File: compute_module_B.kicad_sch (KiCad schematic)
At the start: 3 parts

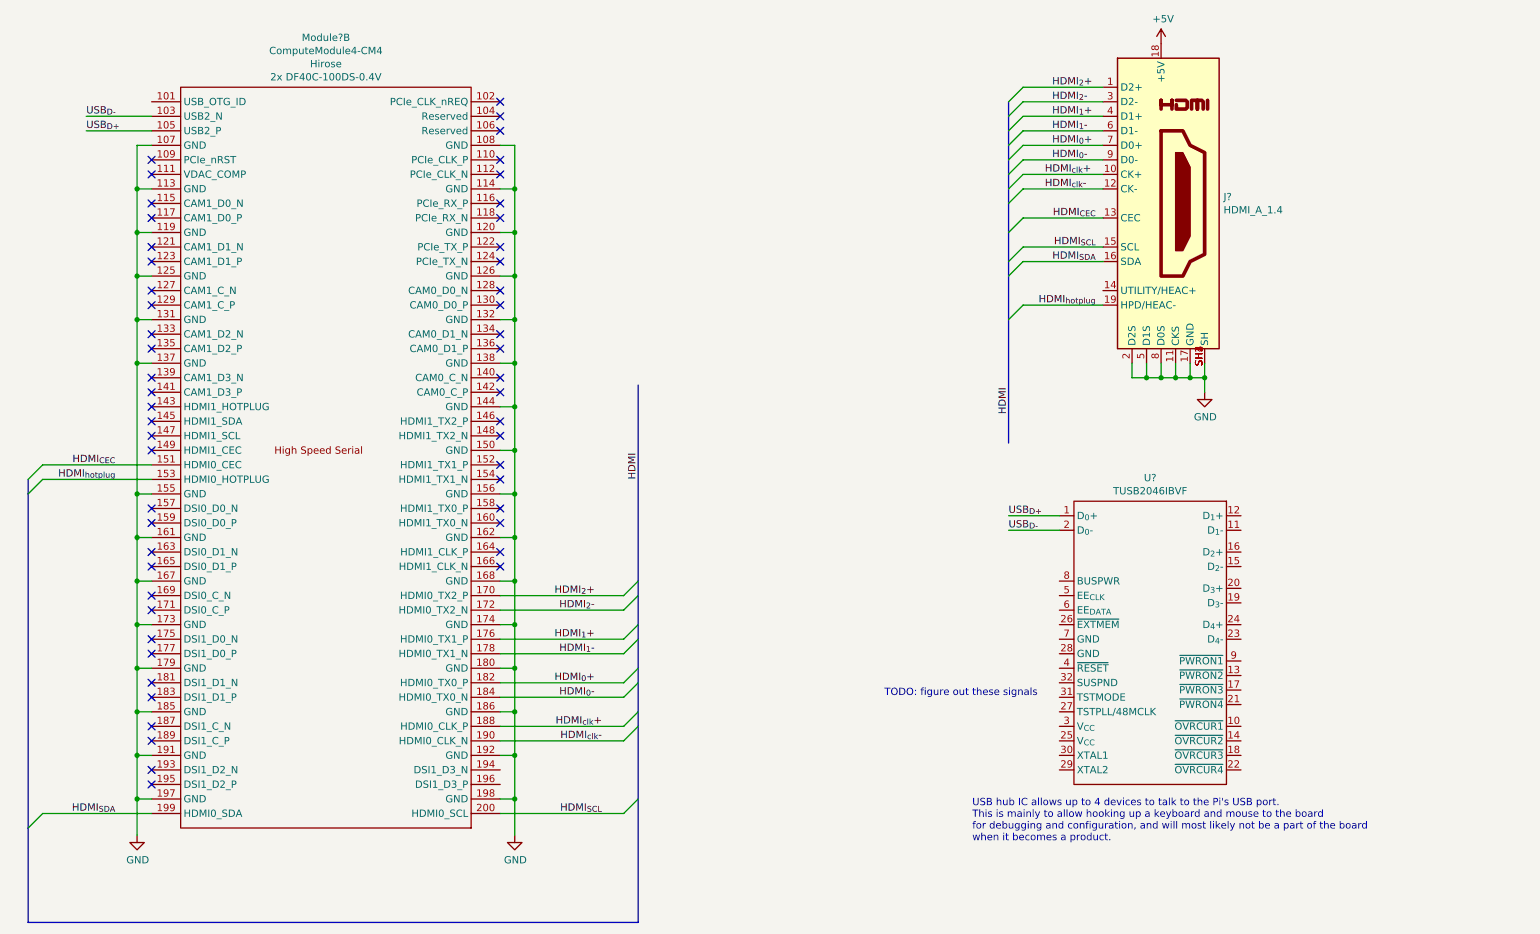
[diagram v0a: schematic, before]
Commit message: Added buses and USB ports to schematic
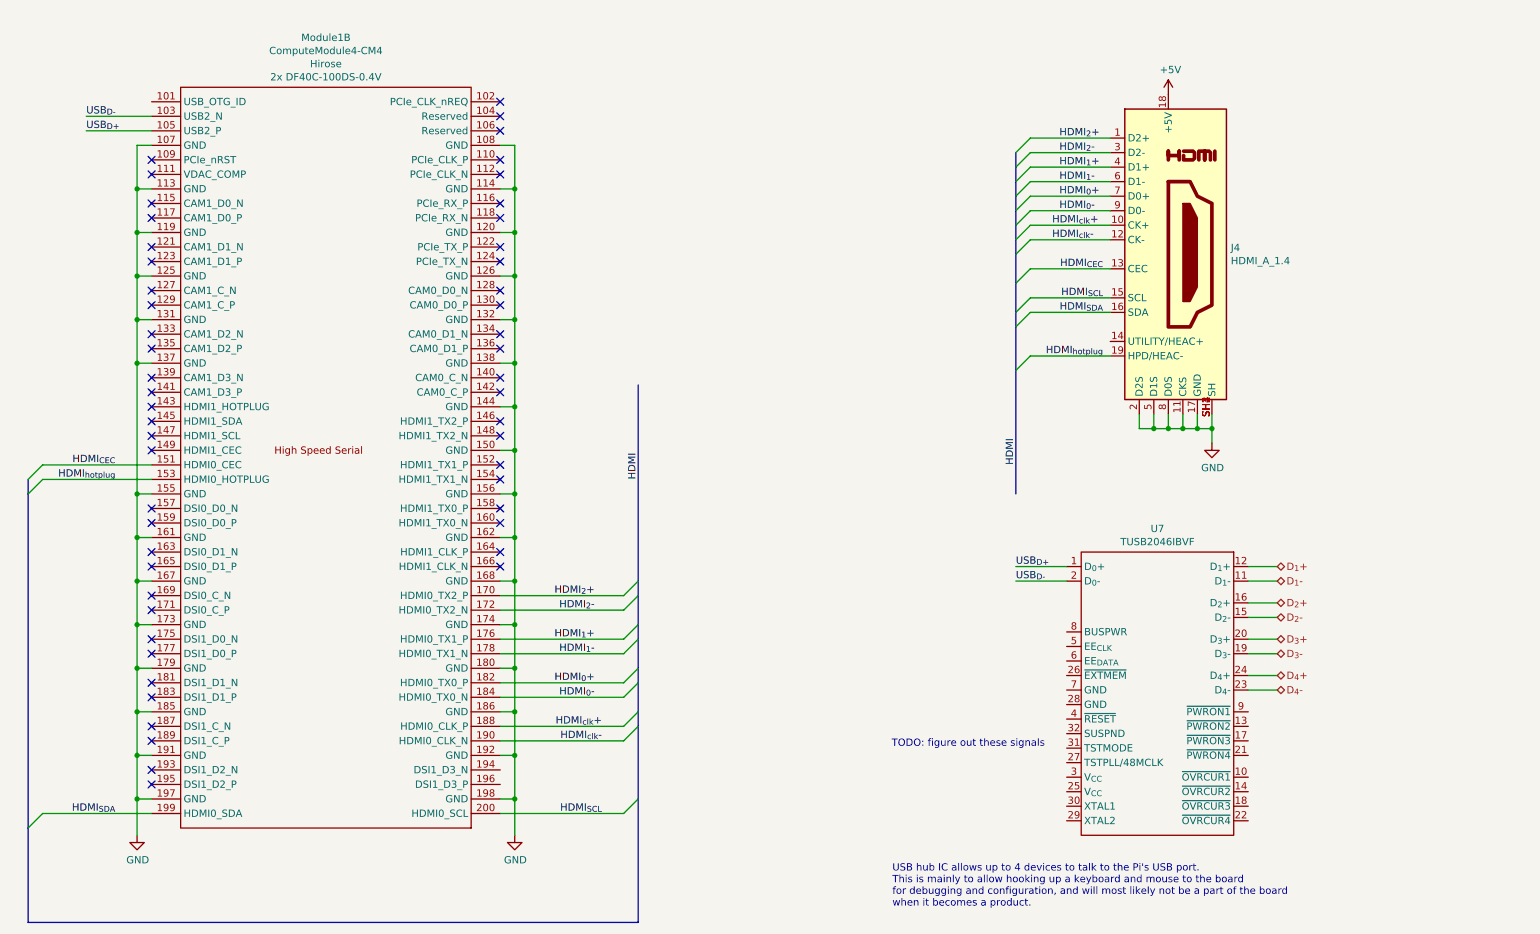
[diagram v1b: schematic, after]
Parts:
- gave numbers to parts that had none: 3
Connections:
- net D_{1}-: now reaches U7.11 (D_{1}-)
- net D_{1}+: now reaches U7.12 (D_{1}+)
- net D_{2}-: now reaches U7.15 (D_{2}-)
- net D_{2}+: now reaches U7.16 (D_{2}+)
- net D_{3}-: now reaches U7.19 (D_{3}-)
- net D_{3}+: now reaches U7.20 (D_{3}+)
- net D_{4}-: now reaches U7.23 (D_{4}-)
- net D_{4}+: now reaches U7.24 (D_{4}+)
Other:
- company: (none) -> eCafe Racer
- title: (none) -> Dennis
- moved on the sheet: J4, U7

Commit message: footprints
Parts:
- J8: renamed from J4; symbol CM4IO:HDMI_A_1.4 -> symbols:HDMI_A_1.4
- renumbered U7 to U8
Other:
- note added: "TODO: make of find footprint"
- moved on the sheet: J8

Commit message: Adding footprints and step files for connectors
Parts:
- J8: footprint (none) -> footprints:HDMI_Molex-2086588131; Drawing (none) -> https://www.molex.com/pdm_docs/sd/2086588131_sd.pdf; Manufacturer (none) -> Molex; Manufacturer Part (none) -> 2086588131; Vendor (none) -> Digikey; Vendor Part (none) -> 900-2086588131CT-ND
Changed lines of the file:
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@@
   (junction (at 232.41 88.9) (diameter 0.9144) (color 0 0 0 0))
   (junction (at 234.95 88.9) (diameter 0.9144) (color 0 0 0 0))
+  (no_connect (at 114.3 34.29))
+  (no_connect (at 114.3 67.31))
+  (no_connect (at 114.3 102.87))
+  (no_connect (at 114.3 97.79))
+  (no_connect (at 114.3 52.07))
+  (no_connect (at 53.34 133.35))
+  (no_connect (at 114.3 95.25))
+  (no_connect (at 53.34 82.55))
+  (no_connect (at 53.34 105.41))
+  (no_connect (at 53.34 90.17))
+  (no_connect (at 53.34 102.87))
+  (no_connect (at 53.34 67.31))
+  (no_connect (at 114.3 80.01))
+  (no_connect (at 114.3 41.91))
+  (no_connect (at 114.3 82.55))
+  (no_connect (at 114.3 72.39))
+  (no_connect (at 53.34 49.53))
+  (no_connect (at 114.3 74.93))
+  (no_connect (at 53.34 57.15))
+  (no_connect (at 53.34 59.69))
+  (no_connect (at 53.34 92.71))
+  (no_connect (at 53.34 148.59))
+  (no_connect (at 53.34 120.65))
+  (no_connect (at 114.3 90.17))
+  (no_connect (at 114.3 49.53))
+  (no_connect (at 53.34 143.51))
+  (no_connect (at 53.34 85.09))
+  (no_connect (at 53.34 118.11))
+  (no_connect (at 53.34 135.89))
+  (no_connect (at 114.3 110.49))
+  (no_connect (at 53.34 140.97))
+  (no_connect (at 53.34 44.45))
   (no_connect (at 53.34 52.07))
-  (no_connect (at 114.3 90.17))
-  (no_connect (at 53.34 118.11))
+  (no_connect (at 53.34 125.73))
+  (no_connect (at 53.34 151.13))
+  (no_connect (at 114.3 57.15))
+  (no_connect (at 114.3 44.45))
+  (no_connect (at 114.3 87.63))
+  (no_connect (at 53.34 41.91))
+  (no_connect (at 114.3 64.77))
+  (no_connect (at 53.34 128.27))
+  (no_connect (at 114.3 105.41))
+  (no_connect (at 114.3 113.03))
+  (no_connect (at 53.34 87.63))
+  (no_connect (at 53.34 113.03))
+  (no_connect (at 114.3 36.83))
+  (no_connect (at 53.34 80.01))
+  (no_connect (at 53.34 110.49))
+  (no_connect (at 114.3 59.69))
   (no_connect (at 53.34 64.77))
-  (no_connect (at 53.34 49.53))
-  (no_connect (at 114.3 102.87))
-  (no_connect (at 114.3 41.91))
-  (no_connect (at 114.3 67.31))
-  (no_connect (at 53.34 57.15))
-  (no_connect (at 53.34 85.09))
-  (no_connect (at 53.34 44.45))
-  (no_connect (at 114.3 95.25))
-  (no_connect (at 53.34 148.59))
-  (no_connect (at 53.34 133.35))
-  (no_connect (at 53.34 41.91))
-  (no_connect (at 53.34 128.27))
-  (no_connect (at 53.34 113.03))
-  (no_connect (at 53.34 110.49))
-  (no_connect (at 114.3 110.49))
-  (no_connect (at 53.34 105.41))
-  (no_connect (at 53.34 92.71))
-  (no_connect (at 114.3 74.93))
   (no_connect (at 53.34 74.93))
-  (no_connect (at 53.34 140.97))
-  (no_connect (at 53.34 67.31))
-  (no_connect (at 114.3 34.29))
-  (no_connect (at 114.3 52.07))
-  (no_connect (at 114.3 80.01))
-  (no_connect (at 53.34 143.51))
-  (no_connect (at 114.3 87.63))
-  (no_connect (at 114.3 64.77))
-  (no_connect (at 53.34 151.13))
-  (no_connect (at 53.34 87.63))
-  (no_connect (at 53.34 102.87))
-  (no_connect (at 53.34 80.01))
-  (no_connect (at 114.3 72.39))
-  (no_connect (at 114.3 49.53))
-  (no_connect (at 114.3 36.83))
-  (no_connect (at 114.3 97.79))
-  (no_connect (at 114.3 113.03))
-  (no_connect (at 114.3 44.45))
-  (no_connect (at 53.34 82.55))
-  (no_connect (at 114.3 59.69))
-  (no_connect (at 53.34 135.89))
-  (no_connect (at 53.34 59.69))
+  (no_connect (at 114.3 31.75))
   (no_connect (at 53.34 72.39))
-  (no_connect (at 114.3 82.55))
-  (no_connect (at 114.3 31.75))
-  (no_connect (at 53.34 120.65))
-  (no_connect (at 53.34 90.17))
-  (no_connect (at 53.34 125.73))
-  (no_connect (at 114.3 105.41))
-  (no_connect (at 114.3 57.15))
   (bus_entry (at 31.75 97.79) (size 2.54 -2.54)
     (stroke (width 0.1524) (type solid) (color 0 0 0 0))
@@
       (effects (font (size 1.27 1.27)) (justify left))
     )
-    (property "Footprint" "" (id 2) (at 227.965 58.42 0)
-      (effects (font (size 1.27 1.27)) hide)
-    )
-    (property "Datasheet" "https://en.wikipedia.org/wiki/HDMI" (id 3) (at 227.965 58.42 0)
-      (effects (font (size 1.27 1.27)) hide)
-    )
+    (property "Footprint" "footprints:HDMI_Molex-2086588131" (id 2) (at 227.965 58.42 0)
+      (effects (font (size 1.27 1.27)) hide)
+    )
+    (property "Datasheet" "https://www.molex.com/webdocs/datasheets/pdf/en-us/2086588131_IO_CONNECTORS.pdf" (id 3) (at 227.965 58.42 0)
+      (effects (font (size 1.27 1.27)) hide)
+    )
+    (property "Drawing" "https://www.molex.com/pdm_docs/sd/2086588131_sd.pdf" (id 4) (at 227.33 58.42 0)
+      (effects (font (size 1.27 1.27)) hide)
+    )
+    (property "Vendor" "Digikey" (id 5) (at 227.33 58.42 0)
+      (effects (font (size 1.27 1.27)) hide)
+    )
+    (property "Vendor Part" "900-2086588131CT-ND" (id 6) (at 227.33 58.42 0)
+      (effects (font (size 1.27 1.27)) hide)
+    )
+    (property "Manufacturer" "Molex" (id 7) (at 227.33 58.42 0)
+      (effects (font (size 1.27 1.27)) hide)
+    )
+    (property "Manufacturer Part" "2086588131" (id 8) (at 227.33 58.42 0)
+      (effects (font (size 1.27 1.27)) hide)
+    )

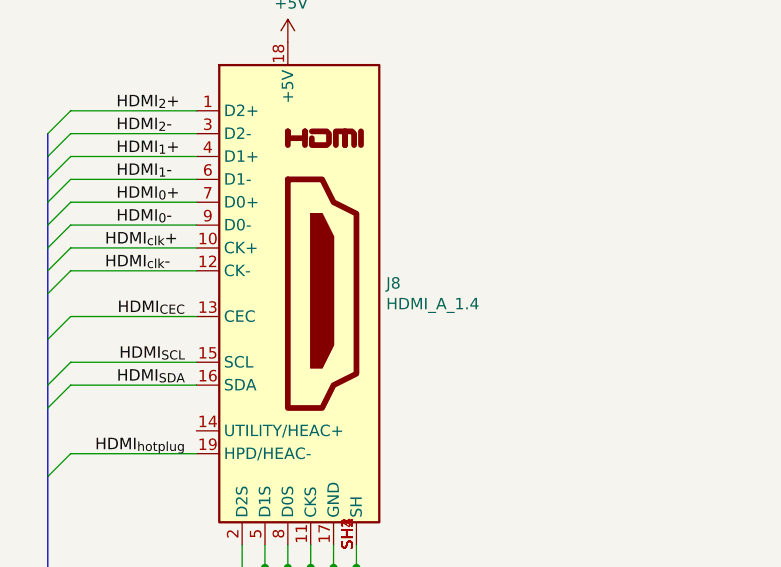
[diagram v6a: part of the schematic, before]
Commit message: footprint assignments
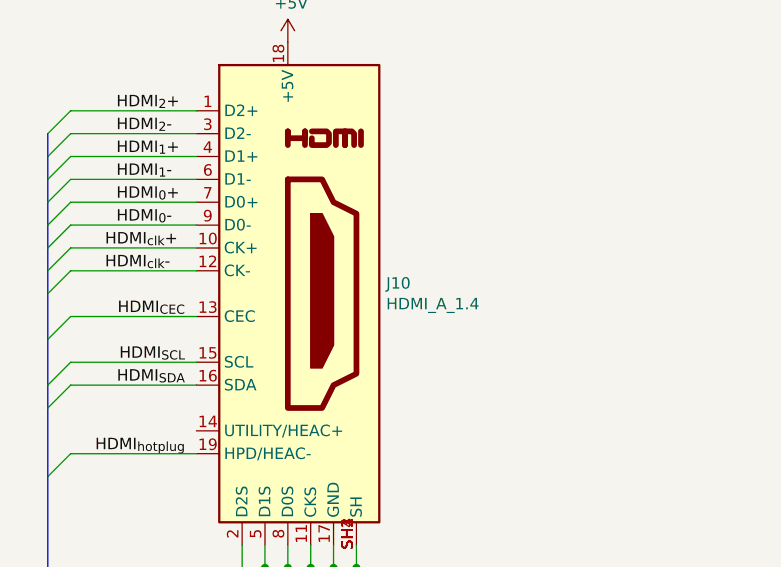
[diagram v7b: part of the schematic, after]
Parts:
- renumbered J8 to J10
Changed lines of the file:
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@@
   (junction (at 232.41 88.9) (diameter 0.9144) (color 0 0 0 0))
   (junction (at 234.95 88.9) (diameter 0.9144) (color 0 0 0 0))
+  (no_connect (at 114.3 87.63))
+  (no_connect (at 53.34 110.49))
+  (no_connect (at 114.3 105.41))
+  (no_connect (at 114.3 90.17))
+  (no_connect (at 53.34 148.59))
+  (no_connect (at 114.3 44.45))
+  (no_connect (at 53.34 140.97))
+  (no_connect (at 53.34 72.39))
+  (no_connect (at 53.34 120.65))
+  (no_connect (at 114.3 80.01))
+  (no_connect (at 114.3 36.83))
+  (no_connect (at 53.34 113.03))
+  (no_connect (at 114.3 110.49))
+  (no_connect (at 114.3 34.29))
+  (no_connect (at 53.34 85.09))
+  (no_connect (at 114.3 67.31))
+  (no_connect (at 114.3 72.39))
+  (no_connect (at 114.3 102.87))
+  (no_connect (at 53.34 49.53))
+  (no_connect (at 114.3 74.93))
+  (no_connect (at 53.34 118.11))
+  (no_connect (at 53.34 135.89))
+  (no_connect (at 53.34 102.87))
+  (no_connect (at 53.34 67.31))
+  (no_connect (at 53.34 92.71))
+  (no_connect (at 114.3 64.77))
+  (no_connect (at 114.3 57.15))
+  (no_connect (at 53.34 44.45))
+  (no_connect (at 114.3 95.25))
+  (no_connect (at 114.3 59.69))
+  (no_connect (at 53.34 133.35))
+  (no_connect (at 114.3 113.03))
+  (no_connect (at 53.34 90.17))
+  (no_connect (at 114.3 97.79))
+  (no_connect (at 53.34 128.27))
+  (no_connect (at 53.34 74.93))
+  (no_connect (at 53.34 52.07))
+  (no_connect (at 53.34 80.01))
+  (no_connect (at 53.34 105.41))
+  (no_connect (at 114.3 49.53))
+  (no_connect (at 53.34 64.77))
+  (no_connect (at 114.3 52.07))
+  (no_connect (at 53.34 151.13))
+  (no_connect (at 53.34 57.15))
+  (no_connect (at 53.34 59.69))
+  (no_connect (at 114.3 82.55))
+  (no_connect (at 114.3 31.75))
+  (no_connect (at 53.34 87.63))
+  (no_connect (at 53.34 41.91))
+  (no_connect (at 114.3 41.91))
   (no_connect (at 53.34 143.51))
-  (no_connect (at 53.34 44.45))
-  (no_connect (at 53.34 64.77))
-  (no_connect (at 53.34 120.65))
-  (no_connect (at 53.34 57.15))
-  (no_connect (at 53.34 118.11))
-  (no_connect (at 114.3 74.93))
-  (no_connect (at 114.3 49.53))
-  (no_connect (at 53.34 133.35))
-  (no_connect (at 114.3 82.55))
-  (no_connect (at 114.3 97.79))
-  (no_connect (at 53.34 59.69))
-  (no_connect (at 114.3 113.03))
-  (no_connect (at 114.3 52.07))
-  (no_connect (at 53.34 72.39))
-  (no_connect (at 53.34 74.93))
-  (no_connect (at 53.34 85.09))
-  (no_connect (at 114.3 31.75))
-  (no_connect (at 114.3 72.39))
-  (no_connect (at 53.34 52.07))
-  (no_connect (at 53.34 148.59))
-  (no_connect (at 114.3 110.49))
-  (no_connect (at 53.34 151.13))
-  (no_connect (at 53.34 92.71))
-  (no_connect (at 114.3 44.45))
-  (no_connect (at 114.3 41.91))
-  (no_connect (at 53.34 140.97))
-  (no_connect (at 53.34 41.91))
-  (no_connect (at 114.3 34.29))
-  (no_connect (at 53.34 135.89))
-  (no_connect (at 53.34 113.03))
-  (no_connect (at 114.3 59.69))
-  (no_connect (at 114.3 102.87))
-  (no_connect (at 53.34 80.01))
-  (no_connect (at 114.3 57.15))
-  (no_connect (at 53.34 67.31))
-  (no_connect (at 53.34 87.63))
-  (no_connect (at 114.3 87.63))
-  (no_connect (at 114.3 105.41))
-  (no_connect (at 114.3 36.83))
+  (no_connect (at 53.34 82.55))
   (no_connect (at 53.34 125.73))
-  (no_connect (at 53.34 105.41))
-  (no_connect (at 114.3 67.31))
-  (no_connect (at 53.34 102.87))
-  (no_connect (at 114.3 80.01))
-  (no_connect (at 53.34 128.27))
-  (no_connect (at 53.34 110.49))
-  (no_connect (at 114.3 95.25))
-  (no_connect (at 53.34 49.53))
-  (no_connect (at 53.34 82.55))
-  (no_connect (at 114.3 90.17))
-  (no_connect (at 53.34 90.17))
-  (no_connect (at 114.3 64.77))
   (bus_entry (at 31.75 97.79) (size 2.54 -2.54)
     (stroke (width 0.1524) (type solid) (color 0 0 0 0))
@@
   (symbol (lib_id "power:+5V") (at 227.33 30.48 0) (unit 1)
     (in_bom yes) (on_board yes)
-    (property "Reference" "#PWR0156" (id 0) (at 227.33 34.29 0)
+    (property "Reference" "#PWR0159" (id 0) (at 227.33 34.29 0)
       (effects (font (size 1.27 1.27)) hide)
     )
@@
   (symbol (lib_id "power:GND") (at 50.8 160.02 0) (unit 1)
     (in_bom yes) (on_board yes)
-    (property "Reference" "#PWR0153" (id 0) (at 50.8 166.37 0)
+    (property "Reference" "#PWR0157" (id 0) (at 50.8 166.37 0)
       (effects (font (size 1.27 1.27)) hide)
     )
@@
   (symbol (lib_id "power:GND") (at 116.84 160.02 0) (unit 1)
     (in_bom yes) (on_board yes)
-    (property "Reference" "#PWR0154" (id 0) (at 116.84 166.37 0)
+    (property "Reference" "#PWR0158" (id 0) (at 116.84 166.37 0)
       (effects (font (size 1.27 1.27)) hide)
     )
@@
   (symbol (lib_id "power:GND") (at 234.95 91.44 0) (unit 1)
     (in_bom yes) (on_board yes)
-    (property "Reference" "#PWR0155" (id 0) (at 234.95 97.79 0)
+    (property "Reference" "#PWR0160" (id 0) (at 234.95 97.79 0)
       (effects (font (size 1.27 1.27)) hide)
     )
@@
   (symbol (lib_id "symbols:HDMI_A_1.4") (at 227.33 58.42 0) (unit 1)
     (in_bom yes) (on_board yes)
-    (property "Reference" "J8" (id 0) (at 238.2521 57.2706 0)
+    (property "Reference" "J10" (id 0) (at 238.2521 57.2706 0)
       (effects (font (size 1.27 1.27)) (justify left))
     )
